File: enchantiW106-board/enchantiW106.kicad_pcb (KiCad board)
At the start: 2 copper layers, 62.2 x 25.4 mm, 66 parts, among them J1 USB_C_Receptacle_USB2.0, SW1 B3U-1000P, SW2 B3U-1000P, U1 USBLC6-2P6, U11 MAX17262REWL+T, U12 BQ25185DLHR, U13 ICM-42670-P, U2 MMC5633NJL, U3 IRIS-W106-00B, U4 NCP167AMX330TBG, U5 CP2102N-Axx-xQFN20, U9 NCP167AMX330TBG

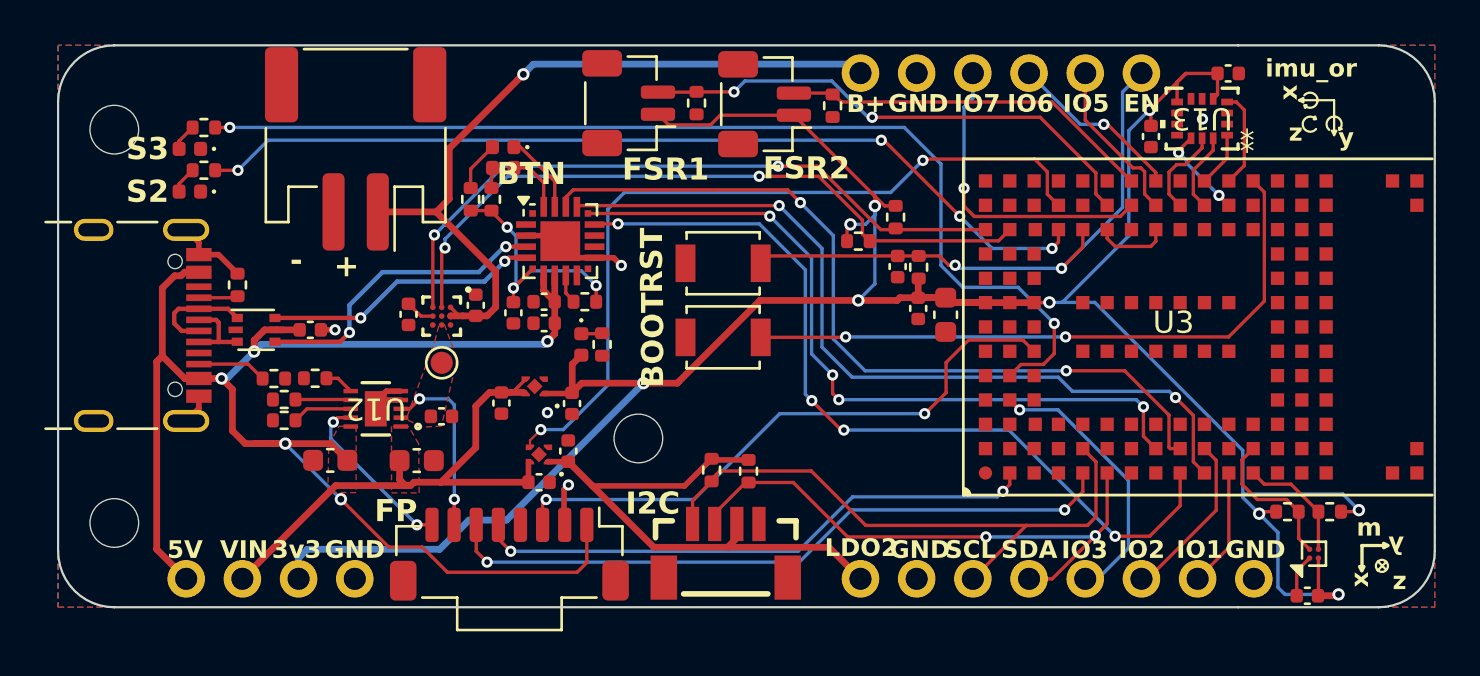
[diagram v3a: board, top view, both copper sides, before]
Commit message: added version of the board with stm32H5 for sensor processing
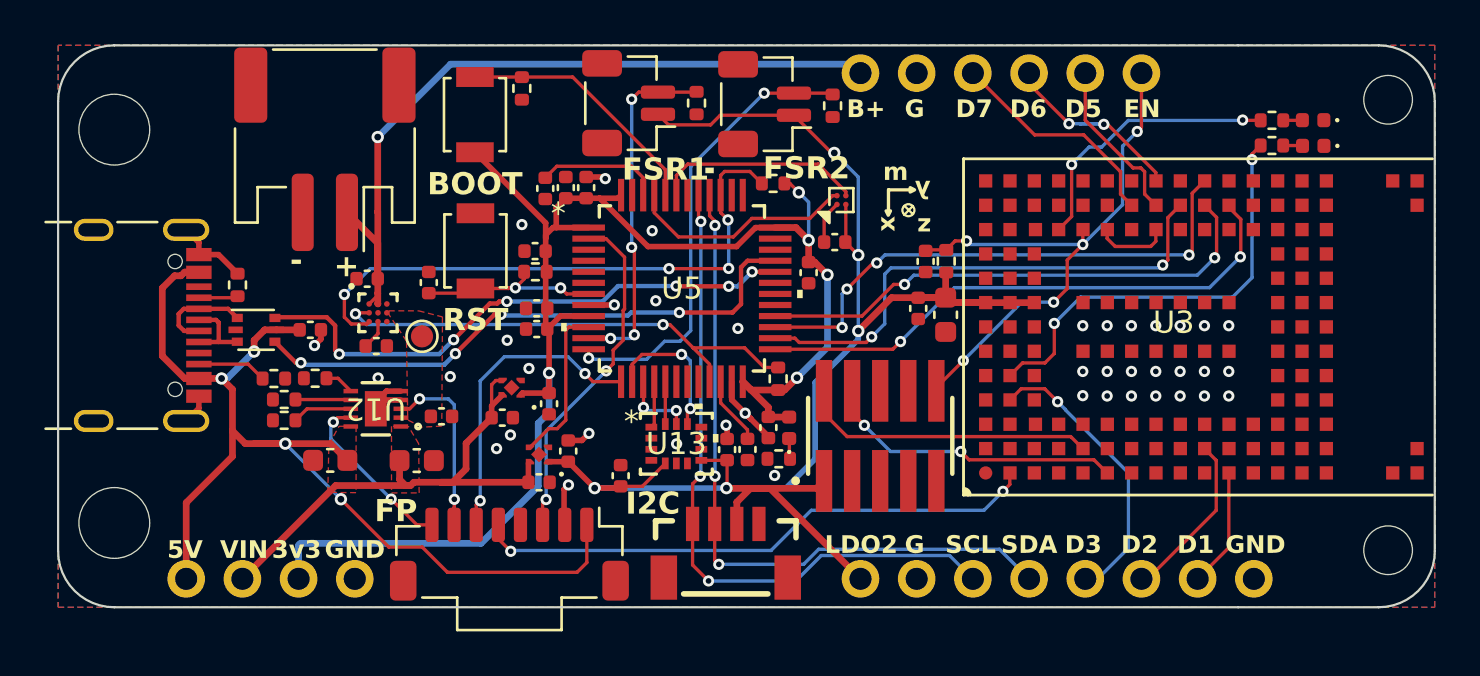
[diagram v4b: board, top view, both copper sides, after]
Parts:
- removed R14, R16, R18: 1k, Resistor_SMD:R_0402_1005Metric
- removed R19, R20: 2k2, Resistor_SMD:R_0402_1005Metric
- removed STATLED3: TX_STAT, LED_SMD:LED_0402_1005Metric
- removed STATLED4: RX_STAT, LED_SMD:LED_0402_1005Metric
- added C10: 4.7uF, Capacitor_SMD:C_0402_1005Metric, F.Cu at (116.6, 54.7)
- added C14: 2.2uF, Capacitor_SMD:C_0402_1005Metric, F.Cu at (123.9, 66.5)
- added C16: 0.1uF, Capacitor_SMD:C_0402_1005Metric, F.Cu at (114.3, 60.1)
- added C20: 0.1uF, Capacitor_SMD:C_0402_1005Metric, F.Cu at (114.3, 57.6)
- added C24: 0.1uF, Capacitor_SMD:C_0402_1005Metric, F.Cu at (126.6, 58.5)
- added C25: 0.1uF, Capacitor_SMD:C_0402_1005Metric, F.Cu at (124.8, 65.5)
- added C26: 0.1uF, Capacitor_SMD:C_0402_1005Metric, F.Cu at (115.7, 54.7)
- added H4: MountingHole, MountingHole:MountingHole_2.2mm_M2, F.Cu at (152.8, 50.7)
- added J3: Programming Header, ENCHANTI_connectors:SAMTEC_FTSH-105-01-F-DV-P-TR, F.Cu at (129.9, 65.9)
- C1, C6: value 0.1uF -> 1uF
- C2: value 0.1uF -> 2.2uF
- H1, H2: footprint MountingHole:MountingHole_2.2mm_M2 -> MountingHole:MountingHole_3.2mm_M3
- R4, R9: value 2k2 -> 10k
- U5: value CP2102N-Axx-xQFN20 -> STM32H523CET6; footprint Package_DFN_QFN:SiliconLabs_QFN-20-1EP_3x3mm_P0.5mm_EP1.8x1.8mm -> ENCHANTI_mcus:LQFP48_STM
- moved STATLED1 50.9 mm to (149.4, 51.6)
- moved STATLED2 50.8 mm to (149.4, 52.8)
- moved R8 48.3 mm to (147.6, 51.6), turned to 0 degrees
- moved R10 48.3 mm to (147.6, 52.8), turned to 0 degrees
- moved R9 41.2 mm to (113.7, 50.2), turned to -90 degrees
- moved R4 35.7 mm to (114.3, 58.5), turned to 0 degrees
- moved H3 34.3 mm to (152.8, 71.1)
- moved C17 28.5 mm to (118.1, 67.7), turned to 90 degrees
- moved C18 28.3 mm to (123.0, 66.5), turned to 90 degrees
- moved U13 27.9 mm to (120.7, 66.3), turned to 0 degrees
- moved C3 26.7 mm to (127.8, 57.2)
- moved U2 26.7 mm to (128.1, 55.3)
- moved SW1 15.1 mm to (111.6, 51.4), turned to -90 degrees
- moved R12 13.1 mm to (125.0, 54.5), turned to 0 degrees
- moved SW2 11.2 mm to (111.6, 57.5), turned to 90 degrees
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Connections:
- ANG1 pad 1: +3V3 -> 3V3_AUX
- ANG3 pad 1: +3V3 -> 3V3_AUX
- BOARDLAYOUT1 pad 2.3: /SCL3 -> /I3C2_SCL
- BOARDLAYOUT1 pad 2.4: /SDA3 -> /I3C2_SDA
- C1 pad 1: VDD -> /NRST
- C13 pad 1: +3V3 -> 3V3_AUX
- C17 pad 1: +3V3 -> 3V3_AUX
- C18 pad 1: +3V3 -> 3V3_AUX
- C19 pad 1: +3V3 -> 3V3_AUX
- C2 pad 1: VUSB -> Net-(C2-Pad1)
- C3 pad 1: +3V3 -> 3V3_AUX
- C6 pad 1: VUSB -> +3V3
- R12 pad 1: /SDA3 -> /I2C2_SDA
- R12 pad 2: 3V3_AUX -> +3V3
- R13 pad 1: /SCL3 -> /I2C2_SCL
- R13 pad 2: 3V3_AUX -> +3V3
- R4 pad 1: /SCL2 -> /NRST
- R5 pad 2: +3V3 -> 3V3_AUX
- R9 pad 1: /SDA2 -> /BOOT0
- R9 pad 2: +3V3 -> GND
- SW1 pad 1: /BOOT -> /BOOT0
- SW1 pad 2: GND -> +3V3
- SW2 pad 1: /EN -> /NRST
- TOUCH1 pad 3: /SDA3 -> /I3C2_SDA
- TOUCH1 pad 4: /SCL3 -> /I3C2_SCL
- U11 pad B1: /SCL -> /I2C2_SCL
- U11 pad C1: /SDA -> /I2C2_SDA
- U13 pad 1: /CIPO -> /SPI1_CIPO
- U13 pad 12: /CS -> /SPI1_CS
- U13 pad 13: /SCLK -> /SPI1_SCLK
- U13 pad 14: /COPI -> /SPI1_COPI
- U13 pad 5: +3V3 -> 3V3_AUX
- U13 pad 8: +3V3 -> 3V3_AUX
- U2 pad A2: /SCL2 -> /I3C1_SCL
- U2 pad B1: +3V3 -> 3V3_AUX
- U2 pad B2: /SDA2 -> /I3C1_SDA
- U3 pad A10: /TXD -> /TX
- U3 pad A12: /SDA2 -> unconnected-(U3A-JTAG_TDO-PadA12)
- U3 pad A5: /LED2 -> unconnected-(U3A-QSPI_RCE-PadA5)
- U3 pad A6: /SDA3 -> /SWDCLK
- U3 pad A9: /CTS -> unconnected-(U3A-SDIO_D1-PadA9)
- U3 pad B12: /SCL2 -> unconnected-(U3A-JTAG_TDI-PadB12)
- U3 pad B5: /SCL3 -> /SWDIO
- U3 pad B8: /RTS -> unconnected-(U3A-SDIO_D0-PadB8)
- U3 pad B9: /RXD -> /RX
- U3 pad F3: /BTN -> unconnected-(U3A-RMII_CLK-PadF3)
- U3 pad H1: +3V3 -> 3V3_AUX
- U3 pad H2: +3V3 -> 3V3_AUX
- U3 pad H3: +3V3 -> 3V3_AUX
- U3 pad L1: /SDA -> unconnected-(U3A-RMII_MDIO-PadL1)
- U3 pad L2: /SCL -> unconnected-(U3A-RMII_MDC-PadL2)
- U3 pad M10: /COPI -> /SPI2_COPI
- U3 pad M11: /CS -> /SPI2_CS
- U3 pad M4: /LDO_EN -> unconnected-(U3A-GPIO[50]-PadM4)
- U3 pad M6: /FSR1 -> unconnected-(U3A-GPIO[46]-PadM6)
- U3 pad M9: /SCLK -> /SPI2_SCLK
- U3 pad N10: /CIPO -> /SPI2_CIPO
- U3 pad N11: /IMU_INT -> unconnected-(U3A-GPIO[1]-PadN11)
- U3 pad N7: /FSR2 -> unconnected-(U3A-GPIO[45]-PadN7)
- U5 pad 1: unconnected-(U5-RS485/GPIO.1-Pad1) -> +3V3
- U5 pad 10: unconnected-(U5-NC-Pad10) -> /LDO_EN
- U5 pad 11: unconnected-(U5-~{SUSPEND}-Pad11) -> /FSR1
- U5 pad 12: GND -> /FSR2
- U5 pad 13: unconnected-(U5-~{WAKEUP}-Pad13) -> /LED2
- U5 pad 14: unconnected-(U5-SUSPEND-Pad14) -> /SPI1_CS
- U5 pad 15: /CTS -> /SPI1_SCLK
- U5 pad 16: /RTS -> /SPI1_CIPO
- U5 pad 17: /TXD -> /SPI1_COPI
- U5 pad 18: /RXD -> unconnected-(U5-PB0-Pad18)
- U5 pad 19: Net-(STATLED4-K) -> unconnected-(U5-PB1-Pad19)
- U5 pad 2: unconnected-(U5-CLK/GPIO.0-Pad2) -> /BTN
- U5 pad 20: Net-(STATLED3-K) -> unconnected-(U5-PB2-Pad20)
- U5 pad 21: GND -> /I2C2_SCL
- U5 pad 3: GND -> unconnected-(U5-PC14-OSC32_IN-Pad3)
- U5 pad 4: /USBD+ -> unconnected-(U5-PC15-OSC32_OUT-Pad4)
- U5 pad 5: /USBD- -> unconnected-(U5-PH0-OSC_IN-Pad5)
- U5 pad 6: VDD -> unconnected-(U5-PH1-OSC_OUT-Pad6)
- U5 pad 7: VUSB -> /NRST
- U5 pad 8: VUSB -> GND
- U5 pad 9: /RST -> +3V3
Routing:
- net +3V3: track 119.3 -> 68.7 mm, vias 9 -> 5
- net 3V3_AUX: track 25.1 -> 71.5 mm, vias 0 -> 5
- net /CTS: track 37.7 -> 0.00 mm, vias 4 -> 0
- net /TXD: track 37.2 -> 0.00 mm, vias 2 -> 0
- net /RXD: track 36.8 -> 0.00 mm, vias 2 -> 0
- net /RTS: track 33.9 -> 0.00 mm, vias 4 -> 0
- net /I3C2_SDA: track 0.00 -> 31.7 mm, vias 0 -> 3
- net /SCL: track 31.6 -> 0.00 mm, vias 2 -> 0
- net /I3C2_SCL: track 0.00 -> 30.8 mm, vias 0 -> 3
- net /SDA: track 30.7 -> 0.00 mm, vias 2 -> 0
- net /BOOT: track 29.1 -> 0.00 mm, vias 2 -> 0
- net /BLUELED: track 41.4 -> 12.6 mm, vias 4 -> 2
- net /ORANGELED: track 48.1 -> 19.7 mm
- net /LDO_EN: track 35.6 -> 7.28 mm, vias 2 -> 0
- net /SCL3: track 27.8 -> 0.00 mm
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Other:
- board text added: "D1"
- board text added: "D2"
- board text added: "D3"
- board text added: "D5"
- board text added: "D6"
- board text added: "D7"
- board text added: "EnchantiW106 v0.3 2025-01 Albert Niyonsenga"
- board text added: "G"
- board text added: "T-Stick Axis"
- board text added: "X"
- board text added: "Y"
- board text added: "ag"
- board text removed: "BTN"
- board text removed: "EnchantiW106 v0.1 2024-10 Albert Niyonsenga"
- board text removed: "IO1"
- board text removed: "IO2"
- board text removed: "IO3"
- board text removed: "IO5"
- board text removed: "IO6"
- board text removed: "IO7"
- board text removed: "S2"
- board text removed: "S3"
- board text removed: "imu_or"

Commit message: removed stm32 co-processor for simplicity, switched to 1.8V IO, swapped to akm magnetometer
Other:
- board text removed: "2 pin JST-PH Vertical Header"
- board text removed: "2 pin JST-SH Vertical Header"
- board text removed: "4 pin JST-SH Vertical Header"
- board text removed: "Boot Button"
- board text removed: "ESP32-S3 WROOM 2"
- board text removed: "Fuel Gauge"
- board text removed: "ICM20948"
- board text removed: "Indicator LEDs (RED)"
- board text removed: "MCP73871"
- board text removed: "NCP167AMX 180TBG"
- board text removed: "NCP167AMX 330TBG"
- board text removed: "Neopixel"
- board text removed: "Ohmite LVK12 Shunt Resistor"
- board text removed: "Reset Button"
- board text removed: "USB C Receptacle"
- board text removed: "USBLC6-LP6"

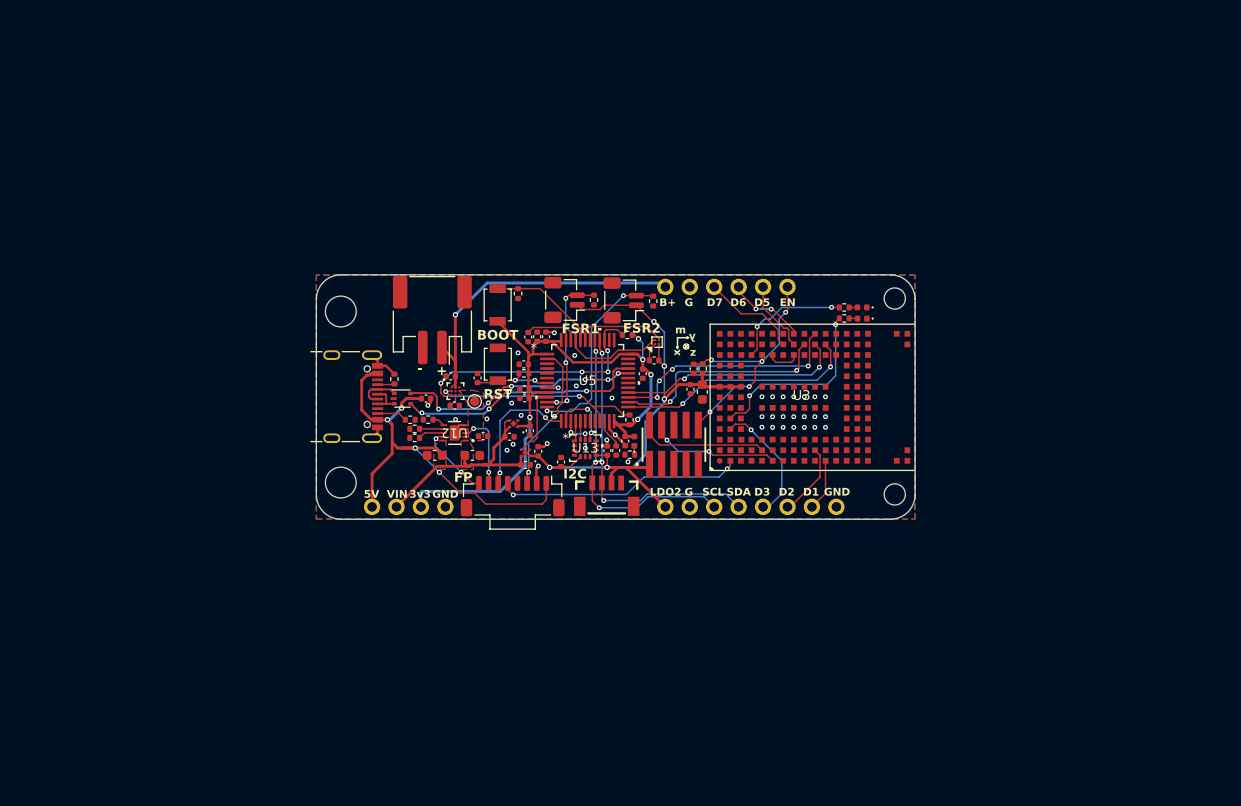
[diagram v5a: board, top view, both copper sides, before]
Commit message: started routing the pcb
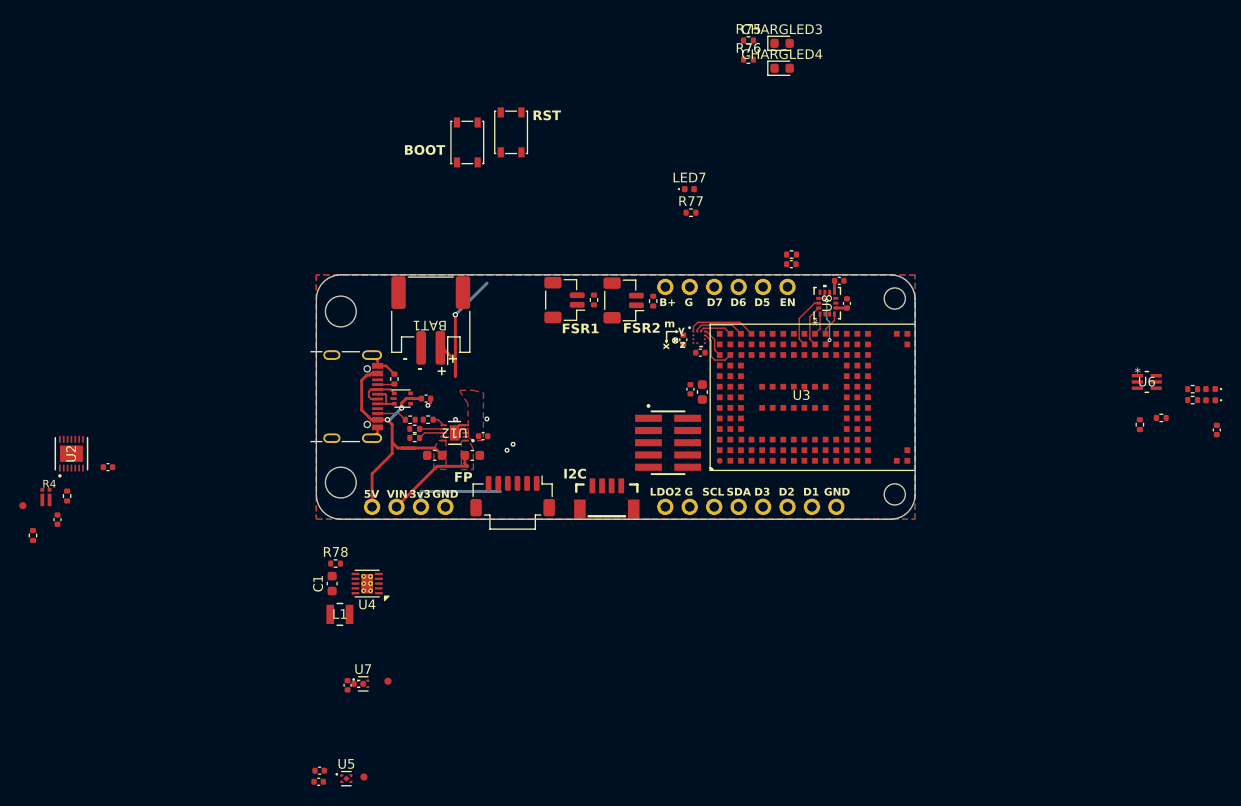
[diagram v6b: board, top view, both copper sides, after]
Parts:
- removed BT1: JST-PH-1x02-2.000mm, Connector_JST:JST_PH_S2B-PH-SM4-TB_1x02-1MP_P2.00mm_Horizontal
- removed C16, C18, C20, C24, C25, C26: 0.1uF, Capacitor_SMD:C_0402_1005Metric
- removed C17: 1uF, Capacitor_SMD:C_0402_1005Metric
- removed CHARGLED1: S1, LED_SMD:LED_0402_1005Metric
- removed TOUCH1: JST-SH-1x04 1.0mm, ENCHANTI_connectors:JST_SMD_1.0mm-4_Vertical
- removed U11: MAX17262REWL+T, ENCHANTI_battery-management:MAX17262
- removed U13: ICM-42670-P, ENCHANTI_MEMS:LGA14_2P5X3X0P91_TDK
- added BAT1: JST_SMD_2.0, ENCHANTI_connectors:Battery_JST_2pin, F.Cu at (104.5, 53.0)
- added CHARGLED3: RED_LED, LED_SMD:LED_0603_1608Metric, F.Cu at (141.1, 24.2)
- added CHARGLED4: YELLOW_LED, LED_SMD:LED_0603_1608Metric, F.Cu at (141.1, 26.8)
- added L1: 2.2uH, ENCHANTI_inductors:DFE252012P-1R0M=P2, F.Cu at (95.2, 83.5)
- added LED7: Green, LED_SMD:LED_0402_1005Metric, F.Cu at (131.5, 39.4)
- added QWIIC2: JST-SH-1x04 1.0mm, ENCHANTI_connectors:JST_SMD_1.0mm-4_Vertical, F.Cu at (122.9, 71.7)
- added R75: 2k, Resistor_SMD:R_0402_1005Metric, F.Cu at (137.6, 23.9)
- added R76: 2k, Resistor_SMD:R_0402_1005Metric, F.Cu at (137.6, 25.9)
- added R77: 2k, Resistor_SMD:R_0402_1005Metric, F.Cu at (131.7, 41.8)
- added R78: 36.5k, Resistor_SMD:R_0402_1005Metric, F.Cu at (94.7, 78.3)
- added TP2: TestPoint, SparkFun-Connector:TestPoint-0.75mm, F.Cu at (100.2, 90.5)
- added TP3: TestPoint, SparkFun-Connector:TestPoint-0.75mm, F.Cu at (97.7, 100.5)
- added U6: SN74LVC2G07DCKR, ENCHANTI_logicICs:Texas_DCK6, F.Cu at (179.0, 59.4)
- added U7: TPS7A20L33PDQNR, ENCHANTI_regulators:Texas_X2SON-4_1x1mm_P0.65mm, F.Cu at (97.6, 90.8)
- added U8: ICM-42670-P, ENCHANTI_MEMS:LGA14_2P5X3X0P91_TDK, F.Cu at (145.8, 51.2)
- C1: value 1uF -> 22uF; footprint Capacitor_SMD:C_0402_1005Metric -> Capacitor_SMD:C_0603_1608Metric
- C10: value 4.7uF -> 1uF
- C12, C5: value 1uF -> 0.1uF
- C14, C2: value 2.2uF -> 0.1uF
- C3: value 220nF -> 0.47uF
- C7: value 0.1uF -> 1uF
- C8: value 0.47uF -> 1uF
- FP2: footprint Connector_Molex:Molex_Pico-Clasp_501331-0807_1x08-1MP_P1.00mm_Vertical -> Connector_Molex:Molex_Pico-Clasp_501331-0607_1x06-1MP_P1.00mm_Vertical
- R12, R13, R3: value 2k2 -> 100k
- R4: value 10k -> 1mOhm; footprint Resistor_SMD:R_0402_1005Metric -> ENCHANTI_resistors:L4CC0306
- R5, R9: value 10k -> 2k2
- SW1, SW2: value B3U-1000P -> PTS810; footprint Button_Switch_SMD:SW_SPST_B3U-1000P -> ENCHANTI_switches:SW_SPST_PTS810
- TP1: footprint TestPoint:TestPoint_Pad_D1.0mm -> SparkFun-Connector:TestPoint-0.75mm
- U2: value MMC5633NJL -> MAX17260SETD+T; footprint Package_BGA:WLP-4_0.86x0.86mm_P0.4mm -> ENCHANTI_battery-management:TDFN-14-EP-ADI
- U4: value NCP167AMX330TBG -> TPS63900; footprint ENCHANTI_regulators:XDFN4_1X1_711AJ_ONS -> Package_SON:WSON-10-1EP_2.5x2.5mm_P0.5mm_EP1.2x2mm_ThermalVias
- U5: value STM32H523CET6 -> TPS7A20L18PDQNR; footprint ENCHANTI_mcus:LQFP48_STM -> ENCHANTI_regulators:Texas_X2SON-4_1x1mm_P0.65mm
- U9: value NCP167AMX330TBG -> AK09940A; footprint ENCHANTI_regulators:XDFN4_1X1_711AJ_ONS -> ENCHANTI_MEMS:LGA11_1p6x1p6x0p58_AKM
- moved C5 70.6 mm to (186.3, 64.4)
- moved R5 67.4 mm to (66.8, 71.2)
- moved U2 62.0 mm to (67.2, 66.8)
- moved C3 57.8 mm to (71.0, 68.2)
- moved R9 56.3 mm to (63.2, 75.3)
- moved R12 56.2 mm to (180.5, 63.1)
- moved R13 53.0 mm to (178.3, 63.8)
- moved C2 52.5 mm to (65.8, 73.7)
- moved R4 51.3 mm to (64.6, 71.3)
- moved U5 48.4 mm to (95.8, 100.6)
- moved TP1 48.2 mm to (62.2, 72.2)
- moved C6 44.2 mm to (93.0, 99.8)
- moved C10 41.7 mm to (96.0, 90.9)
- moved C7 41.6 mm to (147.1, 48.9), turned to 0 degrees
- moved C4 39.3 mm to (93.0, 101.0)
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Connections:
- ANG1 pad 1: 3V3_AUX -> +1V8_AUX
- ANG3 pad 1: 3V3_AUX -> +1V8_AUX
- BOARDLAYOUT1 pad 2.1: 3V3_AUX -> +3V3_AUX
- C1 pad 1: /NRST -> +3V3
- C10 pad 1: +3V3 -> SYS
- C11 pad 1: SYS -> +3V3_AUX
- C12 pad 1: +3V3 -> +1V8_AUX
- C13 pad 1: 3V3_AUX -> +3V3
- C14 pad 1: Net-(C14-Pad1) -> +1V8_AUX
- C19 pad 1: 3V3_AUX -> +3V3
- C2 pad 1: Net-(C2-Pad1) -> +BATT
- C3 pad 1: 3V3_AUX -> /REG
- C5 pad 1: 3V3_AUX -> +1V8_AUX
- C6 pad 1: +3V3 -> +1V8_AUX
- C7 pad 1: +BATT -> +1V8_AUX
- C8 pad 1: /REG -> +1V8_AUX
- FP2 pad 1: VUSB -> GND
- FP2 pad 2: GND -> +3V3_AUX
- FP2 pad 3: /BTN -> VCCIO
- FP2 pad 4: unconnected-(FP2-Pin_4-Pad4) -> /I2C_SDA
- FP2 pad 5: /LED1 -> /I2C_SCL
- FP2 pad 6: /LED2 -> /BUTTON
- J3 pad 1: 3V3_AUX -> VCCIO
- J3 pad 10: /EN -> /JTAG_nRST
- J3 pad 2: /SWDIO -> /JTAG_TMS
- J3 pad 4: /SWDCLK -> /JTAG_TCK
- J3 pad 6: unconnected-(J3-SWO-Pad6) -> /JTAG_TDO
- J3 pad 8: unconnected-(J3-TDI-Pad8) -> /JTAG_TDI
- R10 pad 1: /ORANGELED -> Net-(U6-1Y)
- R10 pad 2: Net-(STATLED2-A) -> Net-(STATLED2-K)
- R12 pad 1: /I2C2_SDA -> +1V8_AUX
- R12 pad 2: +3V3 -> /ORANGELED_EN
- R13 pad 1: /I2C2_SCL -> /BLUELED_EN
- R13 pad 2: +3V3 -> +1V8_AUX
- R3 pad 1: Net-(CHARGLED1-K) -> +3V3
- R3 pad 2: GND -> /EN
- R4 pad 1: /NRST -> +BATT
- R4 pad 2: +3V3 -> CHRG+
- R5 pad 1: /EN -> /I2C_SDA
- R5 pad 2: 3V3_AUX -> +1V8_AUX
- R8 pad 1: /BLUELED -> Net-(U6-2Y)
- R8 pad 2: Net-(STATLED1-A) -> Net-(STATLED1-K)
- R9 pad 1: /BOOT0 -> /I2C_SCL
- R9 pad 2: GND -> +1V8_AUX
- STATLED1 pad 1: GND -> Net-(STATLED1-K)
- STATLED1 pad 2: Net-(STATLED1-A) -> SYS
- STATLED2 pad 1: GND -> Net-(STATLED2-K)
- STATLED2 pad 2: Net-(STATLED2-A) -> SYS
- SW1 pad 1: /BOOT0 -> /EN
- SW1 pad 2: +3V3 -> GND
- SW2 pad 1: /NRST -> /BOOT
- TP1 pad 1: CHRG+ -> +BATT
- U3 pad A10: /TX -> /I2C2_SCL
- U3 pad A12: unconnected-(U3A-JTAG_TDO-PadA12) -> /JTAG_TDO
- U3 pad A14: unconnected-(U3A-JTAG_TMS-PadA14) -> /JTAG_TMS
- U3 pad A2: /LED1 -> unconnected-(U3A-QSPI_RCLK-PadA2)
- U3 pad A6: /SWDCLK -> /I2C_SDA
- U3 pad B11: unconnected-(U3A-JTAG_nRST-PadB11) -> /JTAG_nRST
- U3 pad B12: unconnected-(U3A-JTAG_TDI-PadB12) -> /JTAG_TDI
- U3 pad B14: unconnected-(U3A-JTAG_TCK-PadB14) -> /JTAG_TCK
- U3 pad B5: /SWDIO -> /I2C_SCL
- U3 pad B9: /RX -> /I2C2_SDA
- U3 pad E2: /ORANGELED -> /ORANGELED_EN
- U3 pad F3: unconnected-(U3A-RMII_CLK-PadF3) -> /BUTTON
- U3 pad H1: 3V3_AUX -> +3V3
- U3 pad H2: 3V3_AUX -> +3V3
- U3 pad H3: 3V3_AUX -> +3V3
- U3 pad K1: unconnected-(U3A-RMII_TxD0-PadK1) -> /1V8_EN
- U3 pad L1: unconnected-(U3A-RMII_MDIO-PadL1) -> /MAG_COPI
- U3 pad L2: unconnected-(U3A-RMII_MDC-PadL2) -> /MAG_CIPO
- U3 pad L4: /BLUELED -> /BLUELED_EN
- U3 pad L6: Net-(U3B-+3V3) -> VCCIO
- U3 pad L7: unconnected-(U3B-+1V8-PadL7) -> VCCIO
- U3 pad L8: Net-(U3B-+3V3) -> unconnected-(U3B-+3V3-PadL8)
- U3 pad M10: /SPI2_COPI -> /IMU_COPI
- U3 pad M11: /SPI2_CS -> /IMU_CS
- U3 pad M4: unconnected-(U3A-GPIO[50]-PadM4) -> /3V3_EN
- U3 pad M6: unconnected-(U3A-GPIO[46]-PadM6) -> /FSR2
- U3 pad M9: /SPI2_SCLK -> /IMU_SCLK
- U3 pad N10: /SPI2_CIPO -> /IMU_CIPO
- U3 pad N11: unconnected-(U3A-GPIO[1]-PadN11) -> /IMU_INT
- U3 pad N2: unconnected-(U3A-GPIO[54]-PadN2) -> /MAG_SCLK
- U3 pad N3: unconnected-(U3A-GPIO[53]-PadN3) -> /MAG_CS
- U3 pad N4: unconnected-(U3A-GPIO[51]-PadN4) -> /MAG_INT
- U3 pad N6: unconnected-(U3A-GPIO[47]-PadN6) -> /FSR1
- U4 pad 1: +3V3 -> SYS
- U4 pad 2: GND -> SYS
- U4 pad 3: SYS -> Net-(U4-CFG1)
- U4 pad 4: SYS -> GND
- U5 pad 1: +3V3 -> +1V8_AUX
- U5 pad 2: /BTN -> GND
- U5 pad 3: unconnected-(U5-PC14-OSC32_IN-Pad3) -> /1V8_EN
- U5 pad 4: unconnected-(U5-PC15-OSC32_OUT-Pad4) -> SYS
- U5 pad 5: unconnected-(U5-PH0-OSC_IN-Pad5) -> GND
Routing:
- net 3V3_AUX: track 71.5 -> 0.00 mm, vias 5 -> 0
- net +3V3: track 68.7 -> 9.80 mm, vias 5 -> 0
- net /I3C2_SDA: track 31.7 -> 0.00 mm, vias 3 -> 0
- net /I3C2_SCL: track 30.8 -> 0.00 mm, vias 3 -> 0
- net /EN: track 27.1 -> 0.00 mm, vias 5 -> 0
- net /I2C2_SDA: track 26.7 -> 0.00 mm, vias 4 -> 0
- net /USBD+: track 26.0 -> 0.00 mm, vias 4 -> 0
- net /LED1: track 25.8 -> 0.00 mm, vias 2 -> 0
- net /USBD-: track 25.5 -> 0.00 mm, vias 6 -> 0
- net /SPI2_CS: track 25.3 -> 0.00 mm, vias 2 -> 0
- net /SPI2_CIPO: track 24.6 -> 0.00 mm, vias 4 -> 0
- net /SPI2_COPI: track 23.6 -> 0.00 mm, vias 2 -> 0
- net /SPI2_SCLK: track 23.4 -> 0.00 mm, vias 2 -> 0
- net /I2C2_SCL: track 22.6 -> 0.00 mm, vias 2 -> 0
- net /FSR2: track 20.8 -> 0.00 mm, vias 2 -> 0
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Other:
- board text removed: "1.8V"
- board text removed: "3.3V"
- board text removed: "BAT+"
- board text removed: "SYS"
- board text removed: "T-Stick Axis"
- board text removed: "X"
- board text removed: "Y"
